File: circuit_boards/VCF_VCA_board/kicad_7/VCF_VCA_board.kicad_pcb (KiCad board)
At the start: 2 copper layers, 58.4 x 165.1 mm, 132 parts, among them J1 VCO_BOARD_CON, J2 MOD_BOARD_CON, J3 VCF_EXT_CON, J4 power_entry, SW1 SR1712F-0204, SW2 E-Switch_EG2201, SW3 E-Switch_EG2301, SW4 E-Switch_EG2201, U1 TL072, U2 TL072, U3 TL072, U4 TL072, U5 TL072, U6 TL072, U7 TL072, U707 LM4040DBZ-5, U8 SSI2140, U9 SSI2164

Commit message: Progress on circuit boards
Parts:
- added D101: MMSZ5225B-7-F, Diode_SMD:D_SOD-123, B.Cu at (84.3, 63.4)
- added D102: MMSZ5225B-7-F, Diode_SMD:D_SOD-123, B.Cu at (84.3, 67.8)
- added R103: 1k, Resistor_SMD:R_0603_1608Metric, B.Cu at (89.4, 63.2)
- C301, C302: value ? -> 100p
- R207: value 56k -> 51k
- R311, R312: value ? -> 56k
- R701: value ? -> 2k7
- RV202: value ? -> 5k
- SW2, SW4: value E-Switch_EG2201 -> E-Switch_EG2201B
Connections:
- R506 pad 1: /VCF -> /envelope_VCA/SIGNAL_IN
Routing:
- net /envelope_VCA/SIGNAL_IN: track 0.00 -> 27.4 mm
- net /VCF: track 43.1 -> 21.2 mm
- net Net-(D101-A): track 0.00 -> 4.45 mm
- net /EXT_CV: track 201.8 -> 200.9 mm
- net GND: vias 97 -> 104
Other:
- board size 58.4 x 165.1 mm -> 60.3 x 165.1 mm
- board text added: "MICRO-OX VCF/VCA Board rev 0 2023-03-27"
- board text removed: "MICRO-OX VCF/VCA Board rev 0 2023-03-21"

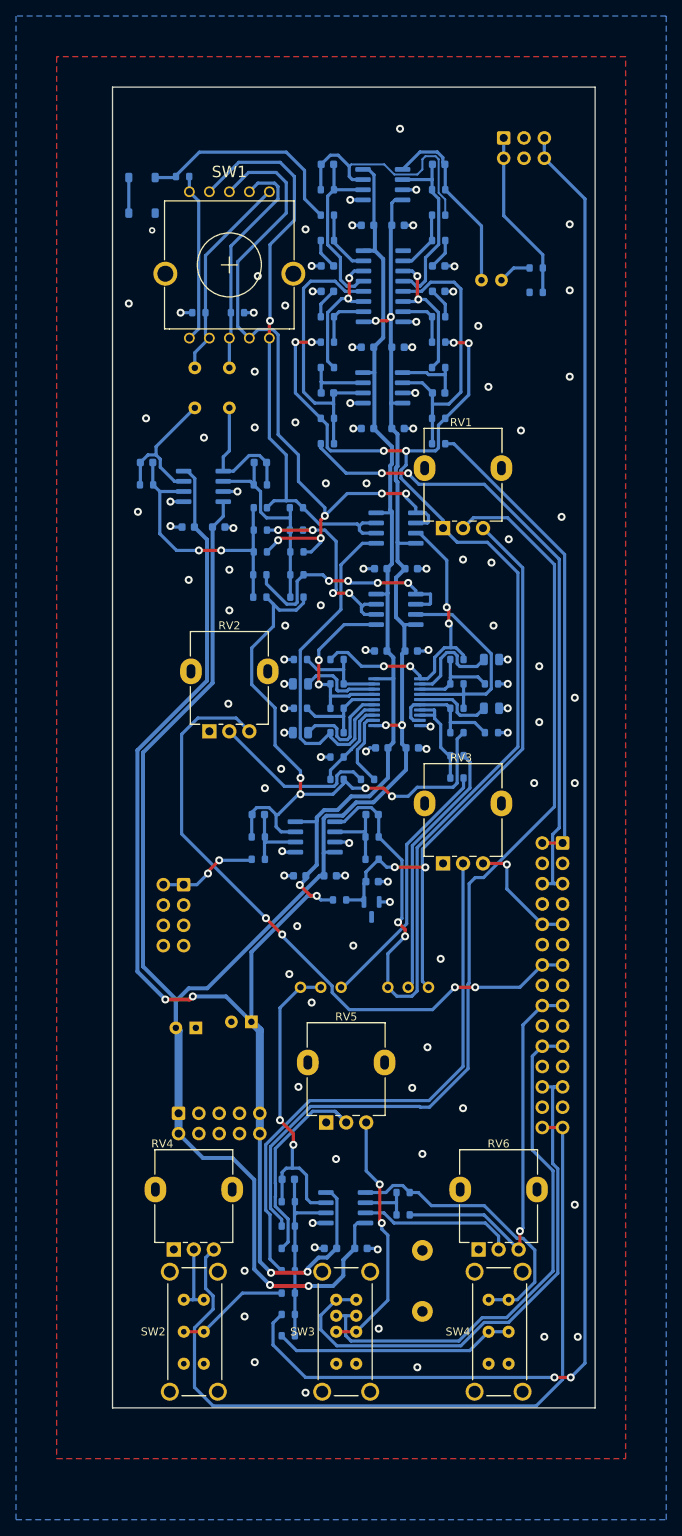
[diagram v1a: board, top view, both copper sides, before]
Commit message: Update PCBs, tweak vals, add VCF CV from DAC
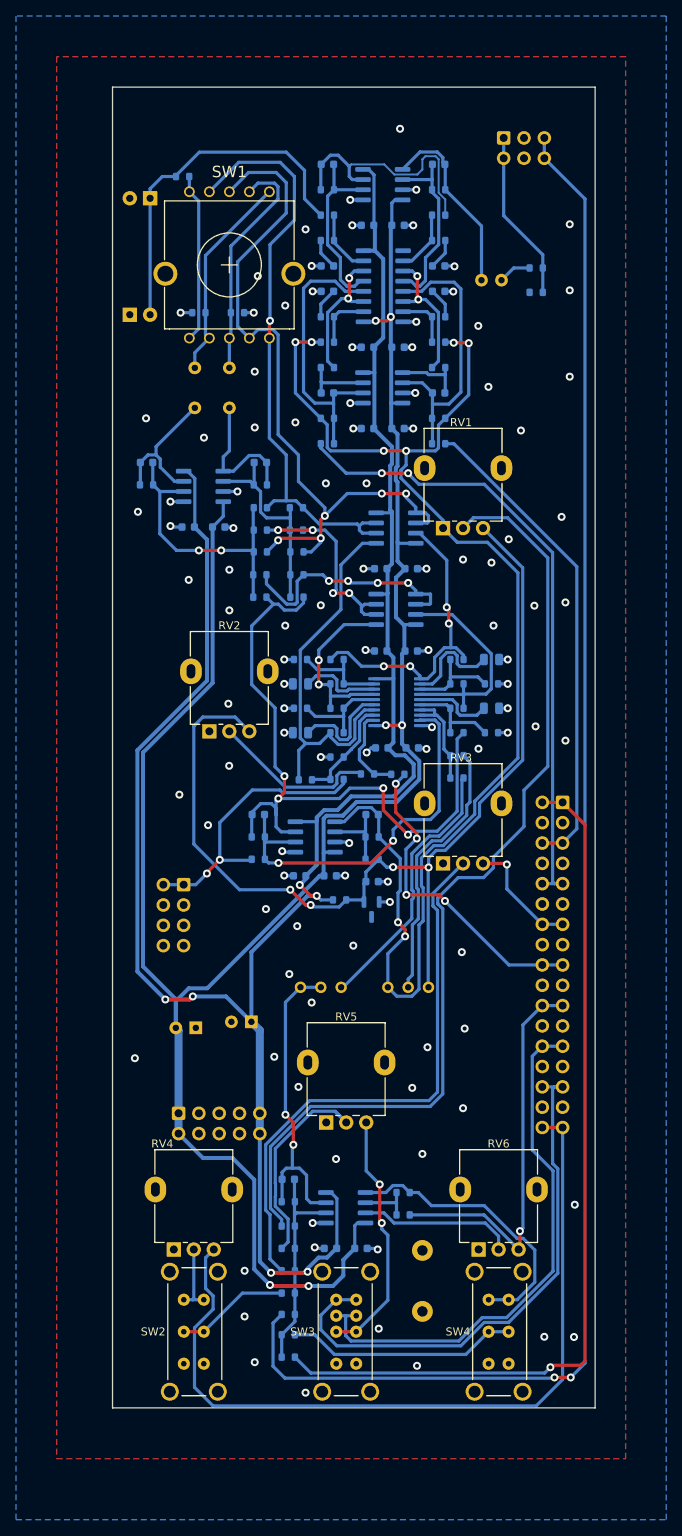
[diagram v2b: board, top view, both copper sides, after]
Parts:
- added R220: 15k, Resistor_SMD:R_0603_1608Metric, B.Cu at (116.3, 138.0)
- added R221: 7k5, Resistor_SMD:R_0603_1608Metric, B.Cu at (104.7, 138.7)
- added R410: 22k, Resistor_SMD:R_0603_1608Metric, B.Cu at (102.6, 210.8)
- C303, C304: value 100n -> 220n
- D101, D102: value MMSZ5225B-7-F -> LED; footprint Diode_SMD:D_SOD-123 -> LED_THT:LED_D5.0mm
- J2: footprint custom_footprints:30_pin_IDC-Header -> custom_footprints:34_pin_IDC_header
- R219: value 6k8 -> 33k
- R311, R312: value 56k -> 18k
- R407: value 100k -> 22k
- R502, R602: value 100k -> 51k
- moved D101 17.2 mm to (82.8, 80.5), turned to 0 degrees
- moved J2 5.08 mm to (136.9, 141.5)
- moved D102 2.11 mm to (85.3, 66.0)
- moved R219 0.68 mm to (112.5, 137.9), turned to 180 degrees
- moved R407 0.13 mm to (102.6, 208.0), turned to 0 degrees
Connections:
- D101 pad 1: /envelope_VCA/SIGNAL_IN -> GND
- D101 pad 2: Net-(D101-A) -> /envelope_VCA/SIGNAL_IN
- D102 pad 1: GND -> /envelope_VCA/SIGNAL_IN
- D102 pad 2: Net-(D101-A) -> GND
- J2 pad 1: /VOLUME_CV -> /VCF_FREQ_CV
- J2 pad 10: /1V_PER_OCT -> /VCA_ENV
- J2 pad 13: /FEEDBACK_CV -> /1V_PER_OCT
- J2 pad 14: /FEEDBACK_CV -> /1V_PER_OCT
- J2 pad 17: /VCF_ENV -> /FEEDBACK_CV
- J2 pad 18: /VCF_ENV -> /FEEDBACK_CV
- J2 pad 2: /VOLUME_CV -> /VCF_FREQ_CV
- J2 pad 21: /S_AND_H_MIXER -> /VCF_ENV
- J2 pad 22: /S_AND_H_MIXER -> /VCF_ENV
- J2 pad 25: /S_AND_H -> /S_AND_H_MIXER
- J2 pad 26: /S_AND_H -> /S_AND_H_MIXER
- J2 pad 29: /MOD_OSC -> /S_AND_H
- J2 pad 30: /MOD_OSC -> /S_AND_H
- J2 pad 5: /VCA_ENV -> /VOLUME_CV
- J2 pad 6: /VCA_ENV -> /VOLUME_CV
- J2 pad 9: /1V_PER_OCT -> /VCA_ENV
- R217 pad 1: /VCF_core/DRY -> /VCF_core/DRY_IN
- RV2 pad 2: Net-(R219-Pad1) -> Net-(R219-Pad2)
- RV2 pad 3: /FEEDBACK_CV -> +5V_REF
- U8 pad 12: Net-(R219-Pad2) -> Net-(R219-Pad1)
- U8 pad 9: Net-(R203-Pad2) -> Net-(U1B--)
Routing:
- net /VCF_FREQ_CV: track 0.00 -> 111.2 mm, vias 0 -> 1
- net +5V_REF: track 79.9 -> 125.7 mm, vias 2 -> 4
- net /FEEDBACK_CV: track 82.1 -> 40.3 mm
- net Net-(U1B--): track 9.52 -> 48.5 mm, vias 0 -> 2
- net /VCF_core/DRY_IN: track 12.5 -> 35.4 mm
- net /envelope_VCA/SIGNAL_IN: track 27.4 -> 45.1 mm
- net Net-(R219-Pad2): track 9.58 -> 20.8 mm
- net Net-(R219-Pad1): track 21.0 -> 10.9 mm
- net /VCF_core/DRY: track 77.7 -> 86.0 mm
- net +12V: track 271.4 -> 276.5 mm
- net Net-(U3B-+): track 43.5 -> 48.4 mm
- net Net-(D101-A): track 4.45 -> 0.00 mm
- net Net-(R203-Pad2): track 15.7 -> 11.9 mm
- net Net-(U5B--): track 23.6 -> 27.0 mm
- net -12V: track 265.8 -> 268.9 mm
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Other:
- board text added: "F CV"
- board text added: "MICRO-OX VCF/VCA Board rev 0.1 2023-04-25"
- board text removed: "MICRO-OX VCF/VCA Board rev 0 2023-03-27"

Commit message: Resistor tweaks while evaluating 1st build
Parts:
- R219: value 33k -> 20k
- R220: value 15k -> 12k
- R307, R308: value 10k -> 30k
- R312: value 18k -> 56k
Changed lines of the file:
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@@
         (effects (font (size 1 1) (thickness 0.15)) (justify mirror))
     )
-    (fp_text value "33k" (at 0 -1.43) (layer "B.Fab")
+    (fp_text value "20k" (at 0 -1.43) (layer "B.Fab")
         (effects (font (size 1 1) (thickness 0.15)) (justify mirror))
     )
@@
         (effects (font (size 1 1) (thickness 0.15)) (justify mirror))
     )
-    (fp_text value "10k" (at 0 -1.43) (layer "B.Fab")
+    (fp_text value "30k" (at 0 -1.43) (layer "B.Fab")
         (effects (font (size 1 1) (thickness 0.15)) (justify mirror))
     )
@@
         (effects (font (size 1 1) (thickness 0.15)) (justify mirror))
     )
-    (fp_text value "18k" (at 0 -1.43) (layer "B.Fab")
+    (fp_text value "56k" (at 0 -1.43) (layer "B.Fab")
         (effects (font (size 1 1) (thickness 0.15)) (justify mirror))
     )
@@
         (effects (font (size 1 1) (thickness 0.15)) (justify mirror))
     )
-    (fp_text value "15k" (at 0 -1.43) (layer "B.Fab")
+    (fp_text value "12k" (at 0 -1.43) (layer "B.Fab")
         (effects (font (size 1 1) (thickness 0.15)) (justify mirror))
     )
@@
         (effects (font (size 1 1) (thickness 0.15)) (justify mirror))
     )
-    (fp_text value "10k" (at 0 -1.43) (layer "B.Fab")
+    (fp_text value "30k" (at 0 -1.43) (layer "B.Fab")
         (effects (font (size 1 1) (thickness 0.15)) (justify mirror))
     )

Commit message: Increase VCF 1v/oct drive so it can be trimmed to play in tune
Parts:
- R207: value 51k -> 47k
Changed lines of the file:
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@@
         (effects (font (size 1 1) (thickness 0.15)) (justify mirror))
     )
-    (fp_text value "51k" (at 0 -1.43) (layer "B.Fab")
+    (fp_text value "47k" (at 0 -1.43) (layer "B.Fab")
         (effects (font (size 1 1) (thickness 0.15)) (justify mirror))
     )

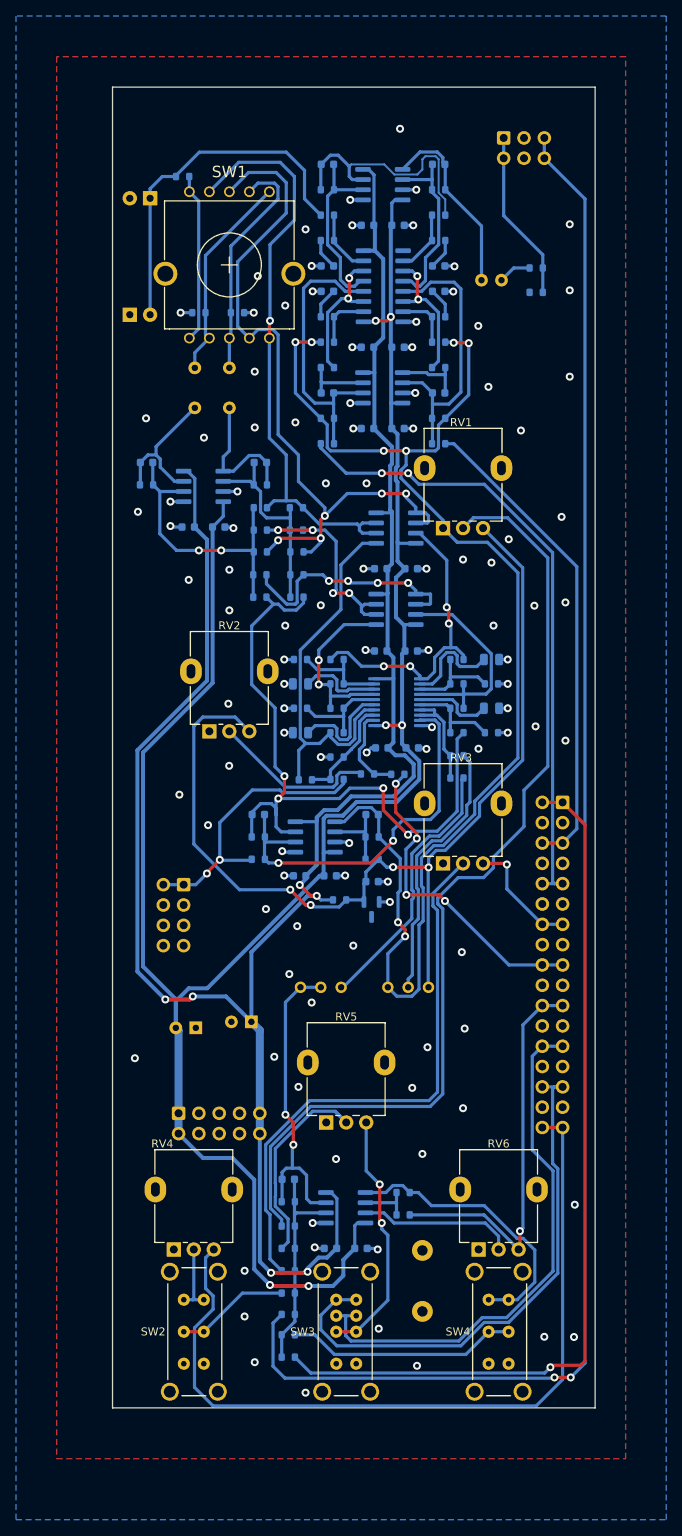
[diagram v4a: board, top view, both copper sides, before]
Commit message: Fix copy paste error with SSI2140 symbol, add potentiometer 3d model
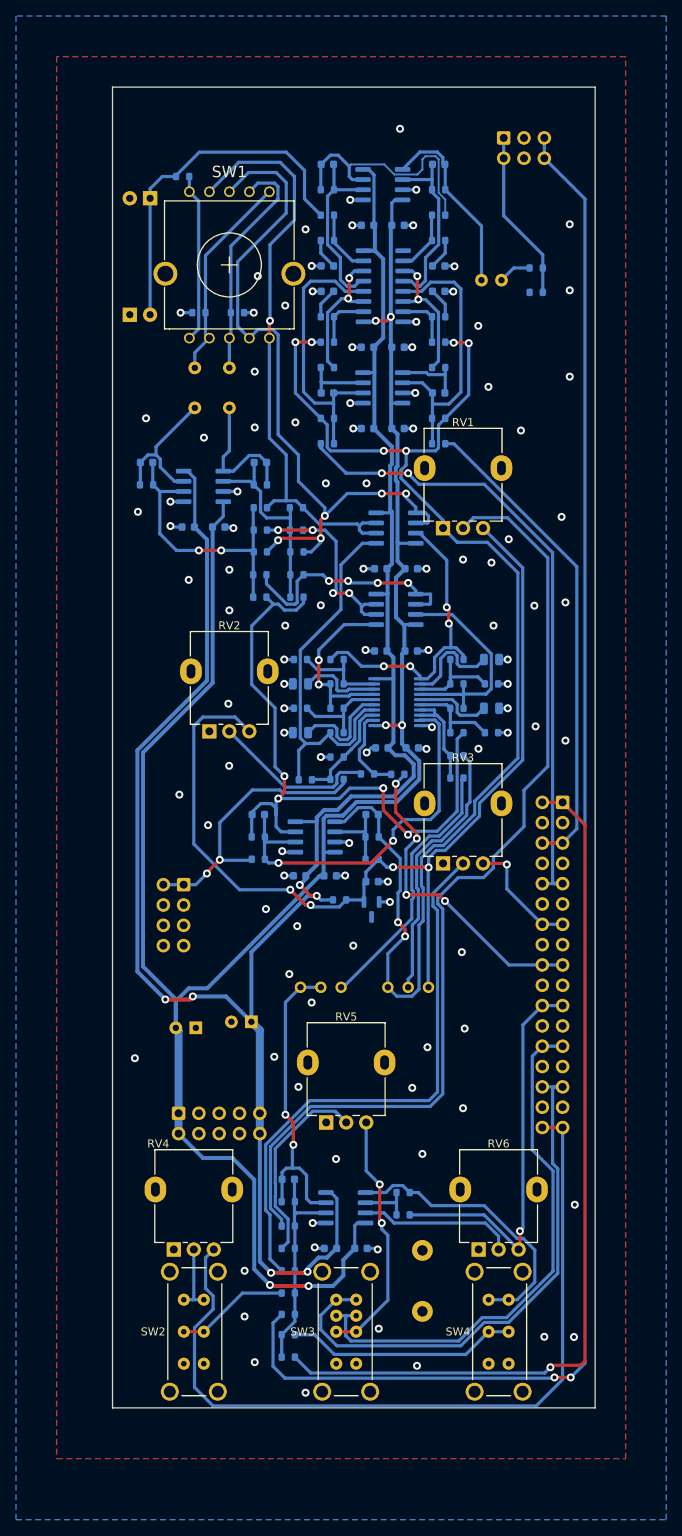
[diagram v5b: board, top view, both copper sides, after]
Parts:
- RV1, RV2, RV3, RV4, RV5, RV6: footprint Potentiometer_THT:Potentiometer_Alpha_RD901F-40-00D_Single_Vertical -> custom_footprints:Potentiometer_Alpha_RD901F-40-00D_Single_Vertical

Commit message: Reduce bandpass gain
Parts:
- R312: value 56k -> 30k
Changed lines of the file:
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@@
         (effects (font (size 1 1) (thickness 0.15)) (justify mirror))
     )
-    (fp_text value "56k" (at 0 -1.43) (layer "B.Fab")
+    (fp_text value "30k" (at 0 -1.43) (layer "B.Fab")
         (effects (font (size 1 1) (thickness 0.15)) (justify mirror))
     )

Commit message: Turn down bandpass gain even more
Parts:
- R312: value 30k -> 18k
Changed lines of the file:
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@@
         (effects (font (size 1 1) (thickness 0.15)) (justify mirror))
     )
-    (fp_text value "30k" (at 0 -1.43) (layer "B.Fab")
+    (fp_text value "18k" (at 0 -1.43) (layer "B.Fab")
         (effects (font (size 1 1) (thickness 0.15)) (justify mirror))
     )

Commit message: Increase gain for hotter output
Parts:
- R508, R608: value 30k -> 47k
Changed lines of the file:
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@@
         (effects (font (size 1 1) (thickness 0.15)) (justify mirror))
     )
-    (fp_text value "30k" (at 0 -1.43) (layer "B.Fab")
+    (fp_text value "47k" (at 0 -1.43) (layer "B.Fab")
         (effects (font (size 1 1) (thickness 0.15)) (justify mirror))
     )
@@
         (effects (font (size 1 1) (thickness 0.15)) (justify mirror))
     )
-    (fp_text value "30k" (at 0 -1.43) (layer "B.Fab")
+    (fp_text value "47k" (at 0 -1.43) (layer "B.Fab")
         (effects (font (size 1 1) (thickness 0.15)) (justify mirror))
     )
